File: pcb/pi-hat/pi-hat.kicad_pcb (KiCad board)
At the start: 2 copper layers, 65 x 56 mm, 5 parts, among them J1 GPIO

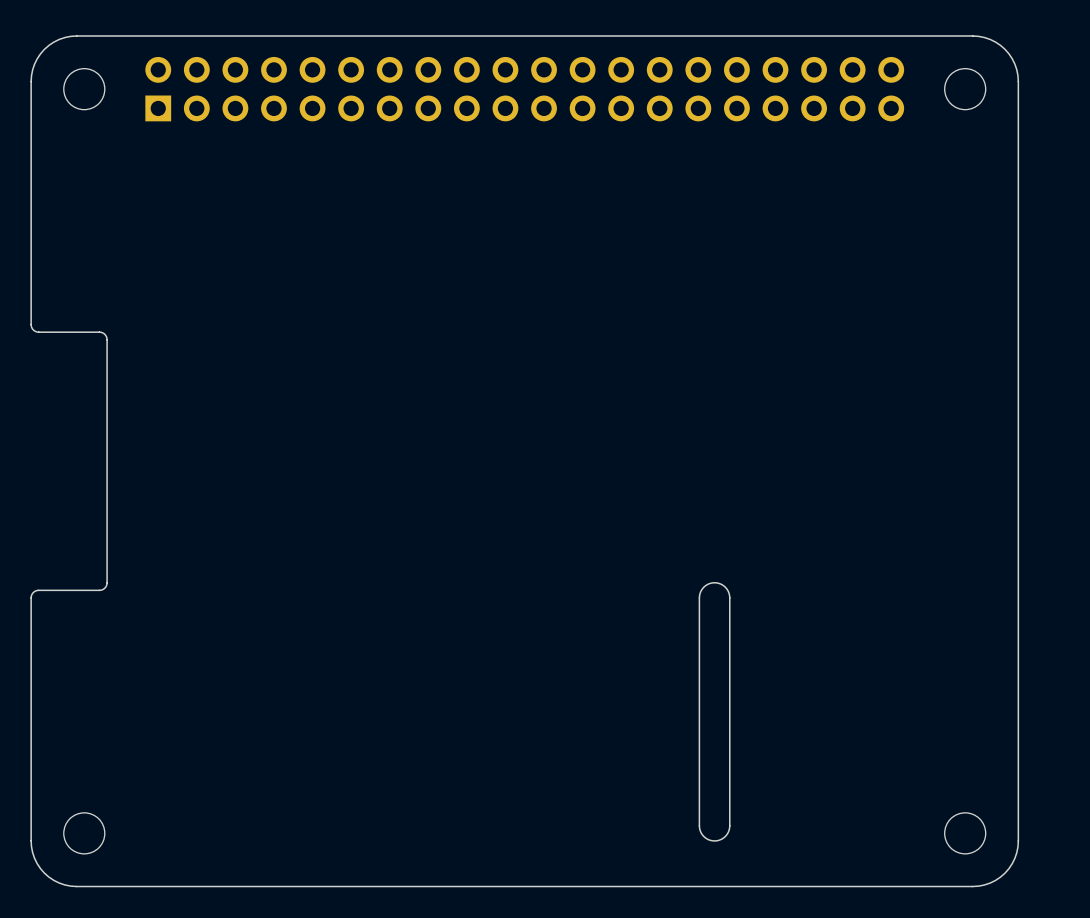
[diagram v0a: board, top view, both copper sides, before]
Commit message: pcb: 3.3V transceiver supply, second Row Bus chain, fab outputs
The THVD1420DR transceivers ran at VCC=5V while driving 3.3V-only GPIOs on
both boards. Per the datasheet the receiver output swings to VCC-0.4V min
(~4.6-4.8V at 5V), and the RX pull-ups went to 5V as well, so both the Pi's
and the RP2350's inputs sat out of spec. Both boards were bodged to 3.3V on
the bench; these schematics bring the sources in line.

pi-hat:
- IC3 supply, decoupling and RX pull-up moved from +5V to +3V3; no +5V net
  remains on the board.
- Second Row Bus chain added (IC4) so the 8 rows split across two chains -
  see docs/row-bus-protocol.md for why one chain no longer fits the frame
  budget. Chain A on uart0 (GPIO14/15), chain B on uart2 (GPIO4/5).
- Both direction lines moved onto the UARTs' own RTS pins, GPIO17 and
  GPIO7, so the kernel's RS-485 mode can eventually drive them with
  hardware timing instead of the host's busy-wait.
- Single RJ45 carries both chains on correctly-paired T568B conductors:
  chain A on pins 1-2, chain B on 3-6, grounds on the blue and brown pairs.

row-controller:
- Both transceivers, the INA220 and its I2C pull-ups moved to +3V3. +5V now
  only feeds the Xiao's VUSB input and the regulator that makes it.
- INA220 VBUS now senses +12V through the 5 mOhm shunt, matching what
  docs/row-bus-protocol.md's POWER command has always claimed it measures;
  it previously sat on the 5V rail and reported ~4.8V.

Also adds v1.0/1.2 gerbers and BOM CSVs, following the existing
gerber-1.1 pattern.

Reviewed the pi-hat netlist in detail - header pins, transceiver
orientation, rails, termination and pairing all check out. The
row-controller and tile changes are carried as-is.

Co-Authored-By: Claude Opus 5 <noreply@anthropic.com>
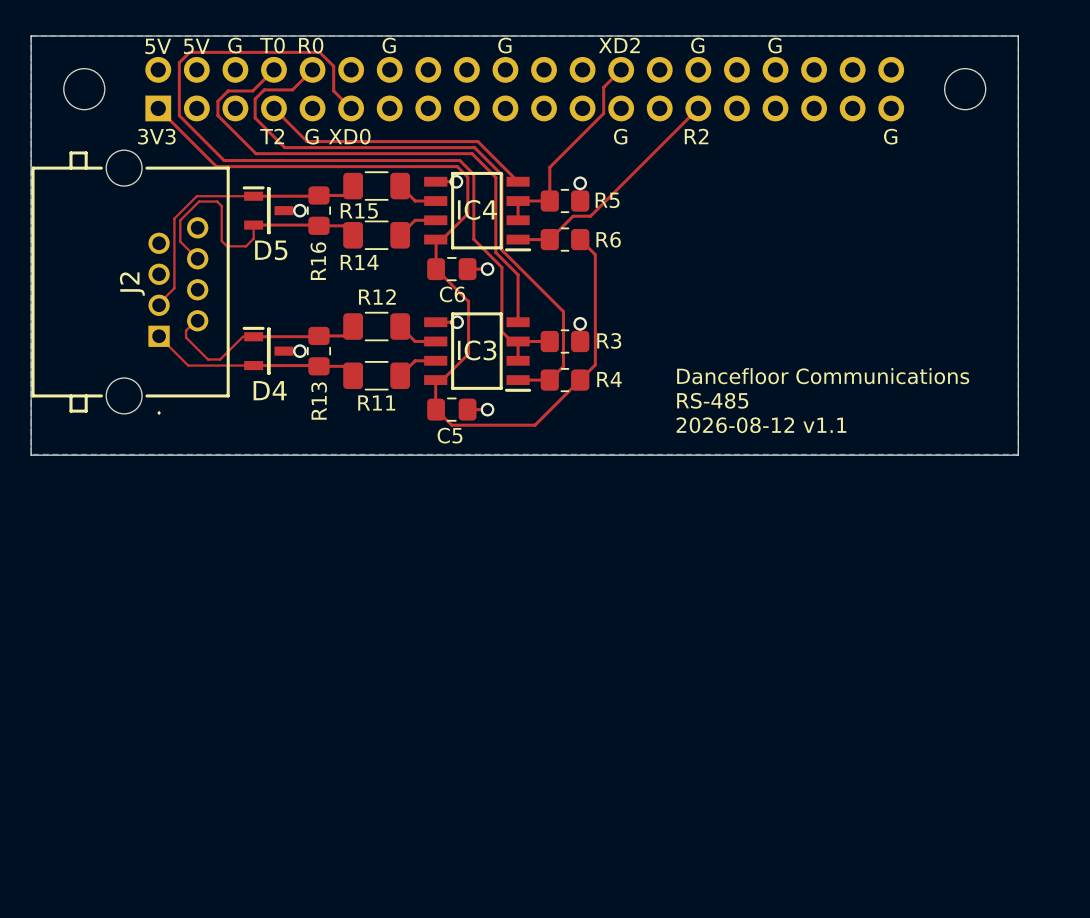
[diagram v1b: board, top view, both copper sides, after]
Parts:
- removed MH3, MH4: MountingHole_2.7mm_M2.5, MountingHole:MountingHole_2.7mm_M2.5
- added C5: 0.1uF, Capacitor_SMD:C_0805_2012Metric_Pad1.18x1.45mm_HandSolder, F.Cu at (127.7, 68.6)
- added C6: 0.1uF, Capacitor_SMD:C_0805_2012Metric_Pad1.18x1.45mm_HandSolder, F.Cu at (127.7, 59.4)
- added D4: CDSOT23-SM712, Garth:SOT95P230X117-3N, F.Cu at (115.7, 64.8)
- added D5: CDSOT23-SM712, Garth:SOT95P230X117-3N, F.Cu at (115.7, 55.5)
- added IC3: THVD1420DR, THVD1420DR:SOIC127P600X175-8N, F.Cu at (129.3, 64.8)
- added IC4: THVD1420DR, THVD1420DR:SOIC127P600X175-8N, F.Cu at (129.3, 55.5)
- added J2: RJ45, Garth:MJ3225880, F.Cu at (108.4, 63.8)
- added R11: 10 Ohms, Resistor_SMD:R_1206_3216Metric_Pad1.30x1.75mm_HandSolder, F.Cu at (122.8, 66.4)
- added R12: 10 Ohms, Resistor_SMD:R_1206_3216Metric_Pad1.30x1.75mm_HandSolder, F.Cu at (122.8, 63.1)
- added R13: 120 Ohms, Resistor_SMD:R_0805_2012Metric_Pad1.20x1.40mm_HandSolder, F.Cu at (119.0, 64.8)
- added R14: 10 Ohms, Resistor_SMD:R_1206_3216Metric_Pad1.30x1.75mm_HandSolder, F.Cu at (122.8, 57.1)
- added R15: 10 Ohms, Resistor_SMD:R_1206_3216Metric_Pad1.30x1.75mm_HandSolder, F.Cu at (122.8, 53.9)
- added R16: 120 Ohms, Resistor_SMD:R_0805_2012Metric_Pad1.20x1.40mm_HandSolder, F.Cu at (119.0, 55.5)
- added R3: 10K, Resistor_SMD:R_0805_2012Metric_Pad1.20x1.40mm_HandSolder, F.Cu at (135.2, 64.1)
- added R4: 10K, Resistor_SMD:R_0805_2012Metric_Pad1.20x1.40mm_HandSolder, F.Cu at (135.2, 66.7)
- added R5: 10K, Resistor_SMD:R_0805_2012Metric_Pad1.20x1.40mm_HandSolder, F.Cu at (135.2, 54.9)
- added R6: 10K, Resistor_SMD:R_0805_2012Metric_Pad1.20x1.40mm_HandSolder, F.Cu at (135.2, 57.4)
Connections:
- J1 pad 11: /GPIO17 -> /XDIR0
- J1 pad 12: /GPIO18/PCM.CLK -> unconnected-(J1-Pin_12-Pad12)
- J1 pad 13: /GPIO27 -> unconnected-(J1-Pin_13-Pad13)
- J1 pad 15: /GPIO22 -> unconnected-(J1-Pin_15-Pad15)
- J1 pad 16: /GPIO23 -> unconnected-(J1-Pin_16-Pad16)
- J1 pad 17: +3V3 -> unconnected-(J1-Pin_17-Pad17)
- J1 pad 18: /GPIO24 -> unconnected-(J1-Pin_18-Pad18)
- J1 pad 19: /GPIO10/SPI0.MOSI -> unconnected-(J1-Pin_19-Pad19)
- J1 pad 2: +5V -> unconnected-(J1-Pin_2-Pad2)
- J1 pad 21: /GPIO9/SPI0.MISO -> unconnected-(J1-Pin_21-Pad21)
- J1 pad 22: /GPIO25 -> unconnected-(J1-Pin_22-Pad22)
- J1 pad 23: /GPIO11/SPI0.SCLK -> unconnected-(J1-Pin_23-Pad23)
- J1 pad 24: /GPIO8/SPI0.CE0 -> unconnected-(J1-Pin_24-Pad24)
- J1 pad 26: /GPIO7/SPI0.CE1 -> /XDIR2
- J1 pad 27: /ID_SDA -> unconnected-(J1-Pin_27-Pad27)
- J1 pad 28: /ID_SCL -> unconnected-(J1-Pin_28-Pad28)
- J1 pad 29: /GPIO5 -> /GPIO5/RXD2
- J1 pad 3: /GPIO2/SDA1 -> unconnected-(J1-Pin_3-Pad3)
- J1 pad 31: /GPIO6 -> unconnected-(J1-Pin_31-Pad31)
- J1 pad 32: /GPIO12/PWM0 -> unconnected-(J1-Pin_32-Pad32)
- J1 pad 33: /GPIO13/PWM1 -> unconnected-(J1-Pin_33-Pad33)
- J1 pad 35: /GPIO19/PCM.FS -> unconnected-(J1-Pin_35-Pad35)
- J1 pad 36: /GPIO16 -> unconnected-(J1-Pin_36-Pad36)
- J1 pad 37: /GPIO26 -> unconnected-(J1-Pin_37-Pad37)
- J1 pad 38: /GPIO20/PCM.DIN -> unconnected-(J1-Pin_38-Pad38)
- J1 pad 4: +5V -> unconnected-(J1-Pin_4-Pad4)
- J1 pad 40: /GPIO21/PCM.DOUT -> unconnected-(J1-Pin_40-Pad40)
- J1 pad 5: /GPIO3/SCL1 -> unconnected-(J1-Pin_5-Pad5)
- J1 pad 7: /GPIO4/GPCLK0 -> /GPIO4/TXD2
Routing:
- net +3V3: track 0.00 -> 62.0 mm
- net /XDIR0: track 0.00 -> 54.4 mm
- net /GPIO15/RXD0: track 0.00 -> 41.3 mm
- net /GPIO14/TXD0: track 0.00 -> 35.6 mm
- net /green_B: track 0.00 -> 18.8 mm
- net /green_A: track 0.00 -> 18.8 mm
- net /GPIO4/TXD2: track 0.00 -> 18.1 mm
- net /GPIO5/RXD2: track 0.00 -> 15.4 mm
- net /XDIR2: track 0.00 -> 13.9 mm
- net /orange_A: track 0.00 -> 13.9 mm
- net /orange_B: track 0.00 -> 13.9 mm
- net GND: track 0.00 -> 9.83 mm, vias 0 -> 8
- net Net-(IC4-B): track 0.00 -> 2.75 mm
- net Net-(IC4-A): track 0.00 -> 2.75 mm
- net Net-(IC3-B): track 0.00 -> 2.75 mm
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- added copper zone on B.Cu, net GND
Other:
- board size 65 x 56 mm -> 65 x 27.6 mm
- board text added: "3V3"
- board text added: "5V"
- board text added: "Dancefloor Communications RS-485 2026-08-12 v1.1"
- board text added: "G"
- board text added: "R0"
- board text added: "R2"
- board text added: "T0"
- board text added: "T2"
- board text added: "XD0"
- board text added: "XD2"
- board text added: "green_A"
- board text added: "green_B"
- board text added: "orange_A"
- board text added: "orange_B"
- board text removed: "CAMERA (OPTIONAL)"
- board text removed: "DISPLAY (OPTIONAL)"
- board text removed: "Extend PCB edge 0.5mm if using SMT header"
- board text removed: "PoE"
- board text removed: "RJ45"
- board text removed: "USB"
